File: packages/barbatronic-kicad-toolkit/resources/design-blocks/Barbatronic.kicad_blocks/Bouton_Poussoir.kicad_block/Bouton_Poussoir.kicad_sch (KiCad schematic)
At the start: 3 parts, among them SW1 Bouton

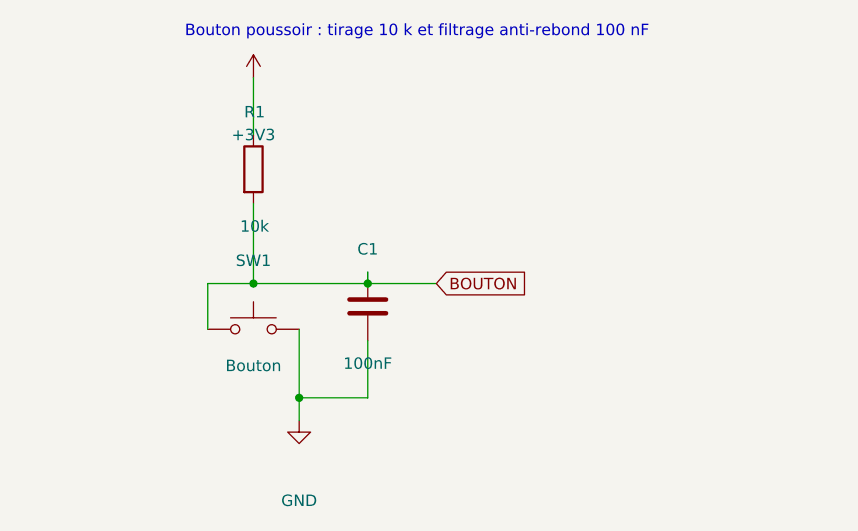
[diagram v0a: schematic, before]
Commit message: Sync docs with hand-edited design blocks
Entree_Alim_Protegee is gone, Servos_x4 is now the reusable single-
output Servos, and Regul_5V is new (78E05, needs the SparkFun PCM
power-symbols package for one symbol). Blocks are now maintained by
hand in KiCad, not generated.

Guard make_design_blocks.py behind --force: it wipes and rebuilds
the whole block library from a now-stale list, which would have
silently destroyed these edits on next run.
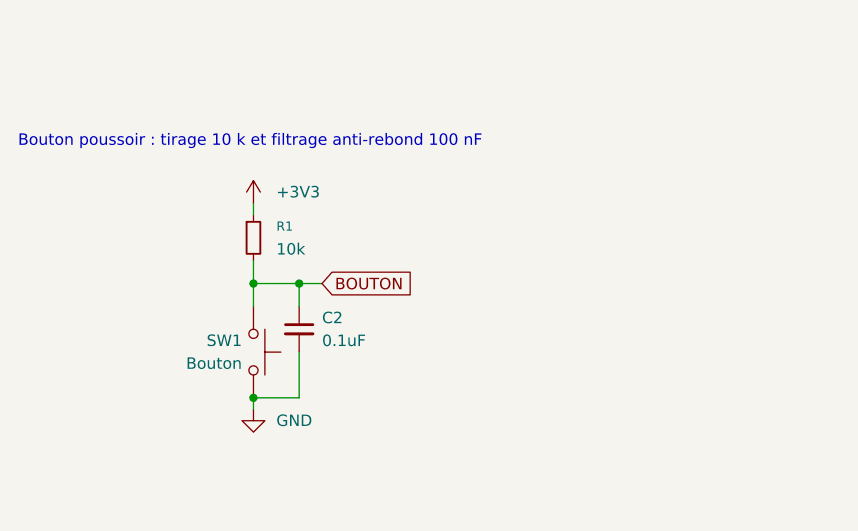
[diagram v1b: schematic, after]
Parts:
- removed C1: 100nF, Capacitor_SMD:C_0805_2012Metric, symbol Device:C
- removed R1: 10k, Resistor_SMD:R_0805_2012Metric, symbol Device:R
- added C2: 0.1uF, Capacitor_SMD:C_1206_3216Metric_Pad1.33x1.80mm_HandSolder, symbol Device:C_Small
- added R1: 10k, Resistor_SMD:R_1206_3216Metric_Pad1.30x1.75mm_HandSolder, symbol Device:R_Small
- SW1: footprint Button_Switch_SMD:SW_SPST_B3U-1000P -> (none)
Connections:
- net +3V3: now also R1.1
- net BOUTON: now also C2.1, R1.2
- net GND: now also C2.2
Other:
- moved on the sheet: SW1
